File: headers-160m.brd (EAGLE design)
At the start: 35.5 x 41.3 mm, 13 parts

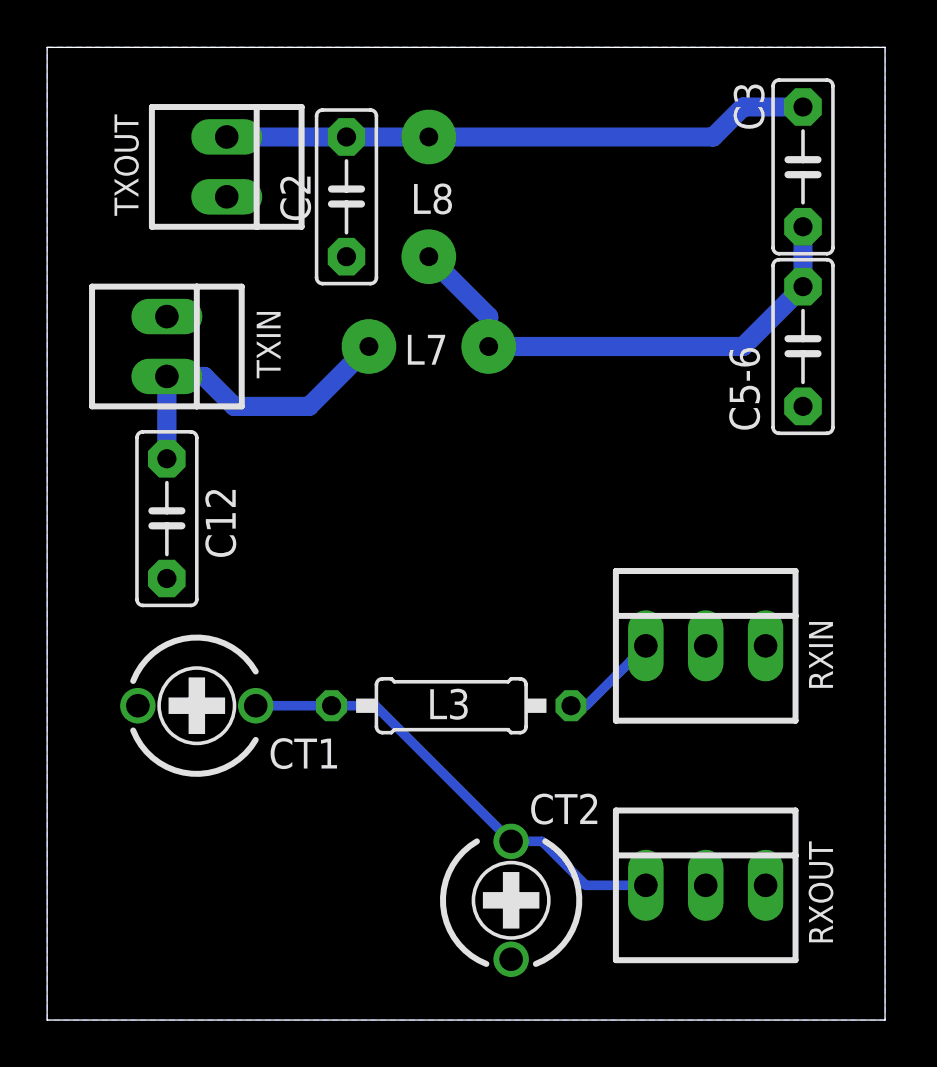
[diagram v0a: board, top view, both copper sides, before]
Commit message: Headers: split C5-6 again, make some TX traces shorter
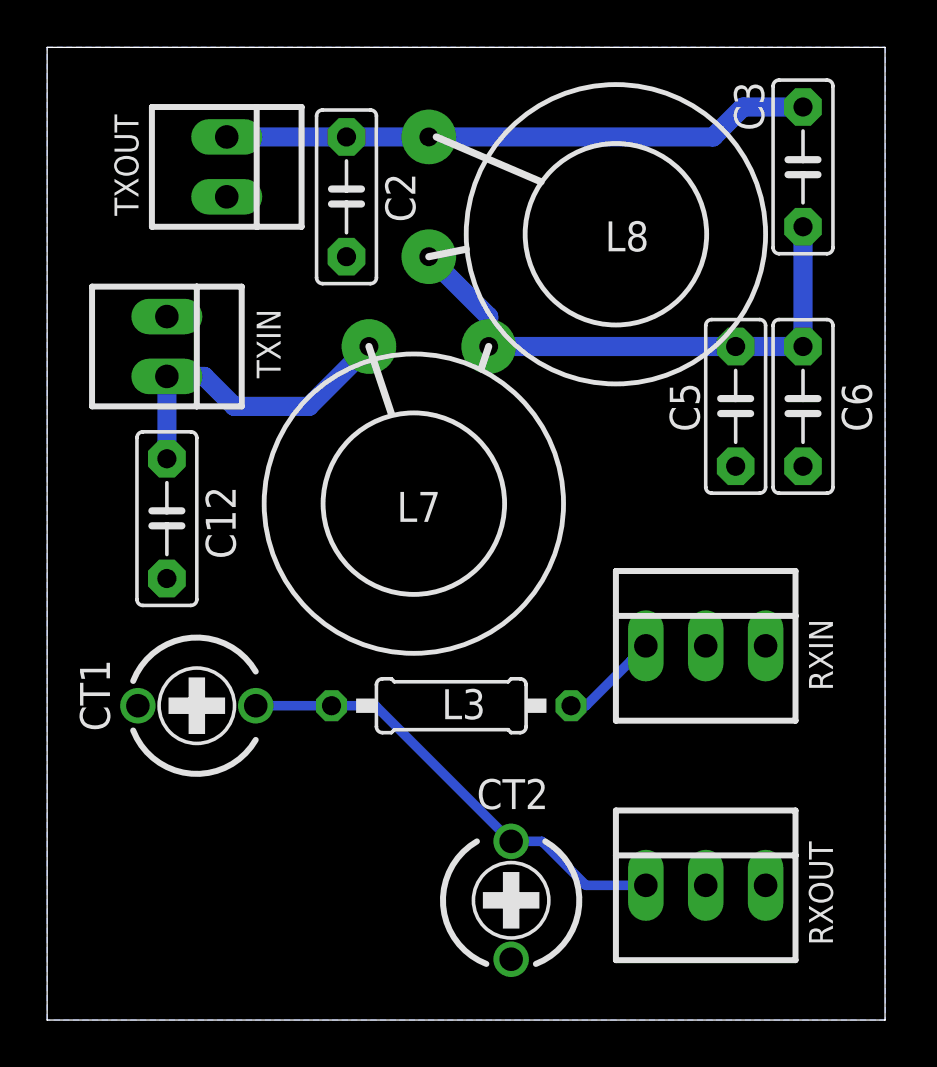
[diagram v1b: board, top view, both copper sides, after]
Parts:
- removed C5-6: 3000p, capacitor-wima:C5B2.5
- added C5, C6: 1500p, capacitor-wima:C5B2.5
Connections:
- net GND: now also C5.1, C6.1, RXIN.2, RXOUT.2, TXIN.1, TXOUT.2; no longer C5-6.1
- net N$5: now also C5.2, C6.2; no longer C5-6.2
